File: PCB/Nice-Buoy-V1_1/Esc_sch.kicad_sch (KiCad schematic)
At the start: 4 parts, among them J401 ESC-BB, J402 ESC-SB

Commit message: HarwareV1.0 frozen Software version 1.1 V1.0 frozen
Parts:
- J401, J402: LCSC C144394 -> C161870
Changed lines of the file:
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@@
     (pin "1")
     (instances
-      (project "Nice-Buoy-V1_0"
+      (project "Nice-Buoy-V1_1"
         (path "/77bea089-a6ae-4a6f-b95b-7a9010ad7c5d/ca10023c-a303-42f5-abd0-839d0a1e9923"
           (reference "#PWR0401") (unit 1)
@@
       (effects (font (size 1.27 1.27)) hide)
     )
-    (property "LCSC" "C144394" (at 135.89 107.95 0)
+    (property "LCSC" "C161870" (at 135.89 107.95 0)
       (effects (font (size 1.27 1.27)) hide)
     )
@@
     (pin "3")
     (instances
-      (project "Nice-Buoy-V1_0"
+      (project "Nice-Buoy-V1_1"
         (path "/77bea089-a6ae-4a6f-b95b-7a9010ad7c5d/ca10023c-a303-42f5-abd0-839d0a1e9923"
           (reference "J402") (unit 1)
@@
     (pin "2")
     (instances
-      (project "Nice-Buoy-V1_0"
+      (project "Nice-Buoy-V1_1"
         (path "/77bea089-a6ae-4a6f-b95b-7a9010ad7c5d/b4716c37-6296-4cc3-83d4-c08b9373ace7"
           (reference "R106") (unit 1)
@@
       (effects (font (size 1.27 1.27)) hide)
     )
-    (property "LCSC" "C144394" (at 135.89 85.09 0)
+    (property "LCSC" "C161870" (at 135.89 85.09 0)
       (effects (font (size 1.27 1.27)) hide)
     )
@@
     (pin "3")
     (instances
-      (project "Nice-Buoy-V1_0"
+      (project "Nice-Buoy-V1_1"
         (path "/77bea089-a6ae-4a6f-b95b-7a9010ad7c5d/ca10023c-a303-42f5-abd0-839d0a1e9923"
           (reference "J401") (unit 1)
@@
     (pin "2")
     (instances
-      (project "Nice-Buoy-V1_0"
+      (project "Nice-Buoy-V1_1"
         (path "/77bea089-a6ae-4a6f-b95b-7a9010ad7c5d/b4716c37-6296-4cc3-83d4-c08b9373ace7"
           (reference "R106") (unit 1)
@@
     (pin "1")
     (instances
-      (project "Nice-Buoy-V1_0"
+      (project "Nice-Buoy-V1_1"
         (path "/77bea089-a6ae-4a6f-b95b-7a9010ad7c5d/ca10023c-a303-42f5-abd0-839d0a1e9923"
           (reference "#PWR0402") (unit 1)

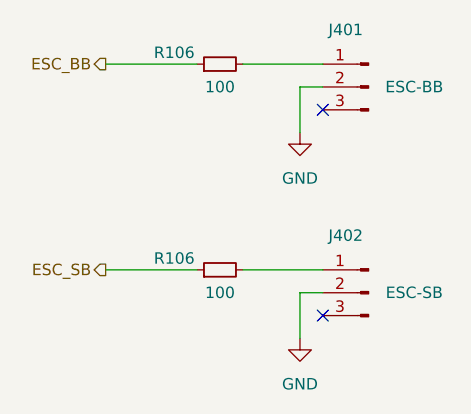
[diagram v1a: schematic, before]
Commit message: Clean up Led status
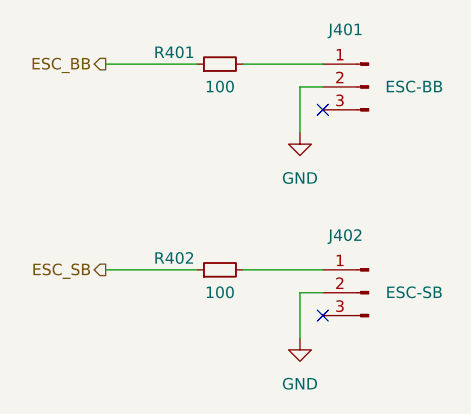
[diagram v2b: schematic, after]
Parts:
- renumbered R106 to R401, R106 to R402

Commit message: Rotation tweaked. Python script gps speed added
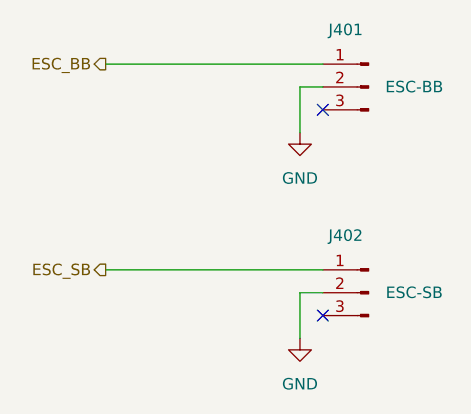
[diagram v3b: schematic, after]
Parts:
- removed R401, R402: 100, A_Device:R_0603, symbol Device:R_Small
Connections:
- net ESC_BB: now also J401.1 (Pin_1)
- net ESC_SB: now also J402.1 (Pin_1)
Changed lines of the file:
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@@
 	(wire
 		(pts
-			(xy 121.92 105.41) (xy 130.81 105.41)
-		)
-		(stroke
-			(width 0)
-			(type default)
-		)
-	)
-	(wire
-		(pts
-			(xy 106.68 82.55) (xy 116.84 82.55)
-		)
-		(stroke
-			(width 0)
-			(type default)
-		)
-	)
-	(wire
-		(pts
-			(xy 106.68 105.41) (xy 116.84 105.41)
-		)
-		(stroke
-			(width 0)
-			(type default)
-		)
-	)
-	(wire
-		(pts
-			(xy 121.92 82.55) (xy 130.81 82.55)
+			(xy 106.68 82.55) (xy 130.81 82.55)
+		)
+		(stroke
+			(width 0)
+			(type default)
+		)
+	)
+	(wire
+		(pts
+			(xy 106.68 105.41) (xy 130.81 105.41)
 		)
 		(stroke
@@
 	)
 	(symbol
-		(lib_id "Device:R_Small")
-		(at 119.38 82.55 90)
-		(unit 1)
-		(exclude_from_sim no)
-		(in_bom yes)
-		(on_board yes)
-		(dnp no)
-		(property "Reference" "R401"
-			(at 114.3 81.28 90)
-			(effects
-				(font
-					(size 1.27 1.27)
-				)
-			)
-		)
-		(property "Value" "100"
-			(at 119.38 85.09 90)
-			(effects
-				(font
-					(size 1.27 1.27)
-				)
-			)
-		)
-		(property "Footprint" "A_Device:R_0603"
-			(at 119.38 82.55 0)
-			(effects
-				(font
-					(size 1.27 1.27)
-				)
-				(hide yes)
-			)
-		)
-		(property "Datasheet" "~"
-			(at 119.38 82.55 0)
-			(effects
-				(font
-					(size 1.27 1.27)
-				)
-				(hide yes)
-			)
-		)
-		(property "Description" ""
-			(at 119.38 82.55 0)
-			(effects
-				(font
-					(size 1.27 1.27)
-				)
-				(hide yes)
-			)
-		)
-		(pin "1"
-		)
-		(pin "2"
-		)
-		(instances
-			(project "Nice-Buoy-V1_1"
-				(path "/77bea089-a6ae-4a6f-b95b-7a9010ad7c5d/ca10023c-a303-42f5-abd0-839d0a1e9923"
-					(reference "R401")
-					(unit 1)
-				)
-			)
-		)
-	)
-	(symbol
 		(lib_id "Connector:Conn_01x03_Pin")
 		(at 135.89 85.09 0)
@@
 					(unit 1)
 				)
-			)
-		)
-	)
-	(symbol
-		(lib_id "Device:R_Small")
-		(at 119.38 105.41 90)
-		(unit 1)
-		(exclude_from_sim no)
-		(in_bom yes)
-		(on_board yes)
-		(dnp no)
-		(property "Reference" "R402"
-			(at 114.3 104.14 90)
-			(effects
-				(font
-					(size 1.27 1.27)
-				)
-			)
-		)
-		(property "Value" "100"
-			(at 119.38 107.95 90)
-			(effects
-				(font
-					(size 1.27 1.27)
-				)
-			)
-		)
-		(property "Footprint" "A_Device:R_0603"
-			(at 119.38 105.41 0)
-			(effects
-				(font
-					(size 1.27 1.27)
-				)
-				(hide yes)
-			)
-		)
-		(property "Datasheet" "~"
-			(at 119.38 105.41 0)
-			(effects
-				(font
-					(size 1.27 1.27)
-				)
-				(hide yes)
-			)
-		)
-		(property "Description" ""
-			(at 119.38 105.41 0)
-			(effects
-				(font
-					(size 1.27 1.27)
-				)
-				(hide yes)
-			)
-		)
-		(pin "1"
-		)
-		(pin "2"
-		)
-		(instances
-			(project "Nice-Buoy-V1_1"
-				(path "/77bea089-a6ae-4a6f-b95b-7a9010ad7c5d/ca10023c-a303-42f5-abd0-839d0a1e9923"
-					(reference "R402")
-					(unit 1)
-				)
